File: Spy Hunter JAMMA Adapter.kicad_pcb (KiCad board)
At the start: 2 copper layers, 111.4 x 135.4 mm, 88 parts, among them P1 1K, P2 1K, P3 10K, P4 1K, SW2 SW_DIP_SPSTx02_Slide_9.78x7.2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, U1 74LS86, U10 NE555, U11 LM386, U12 CD4099B, U2 74LS74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

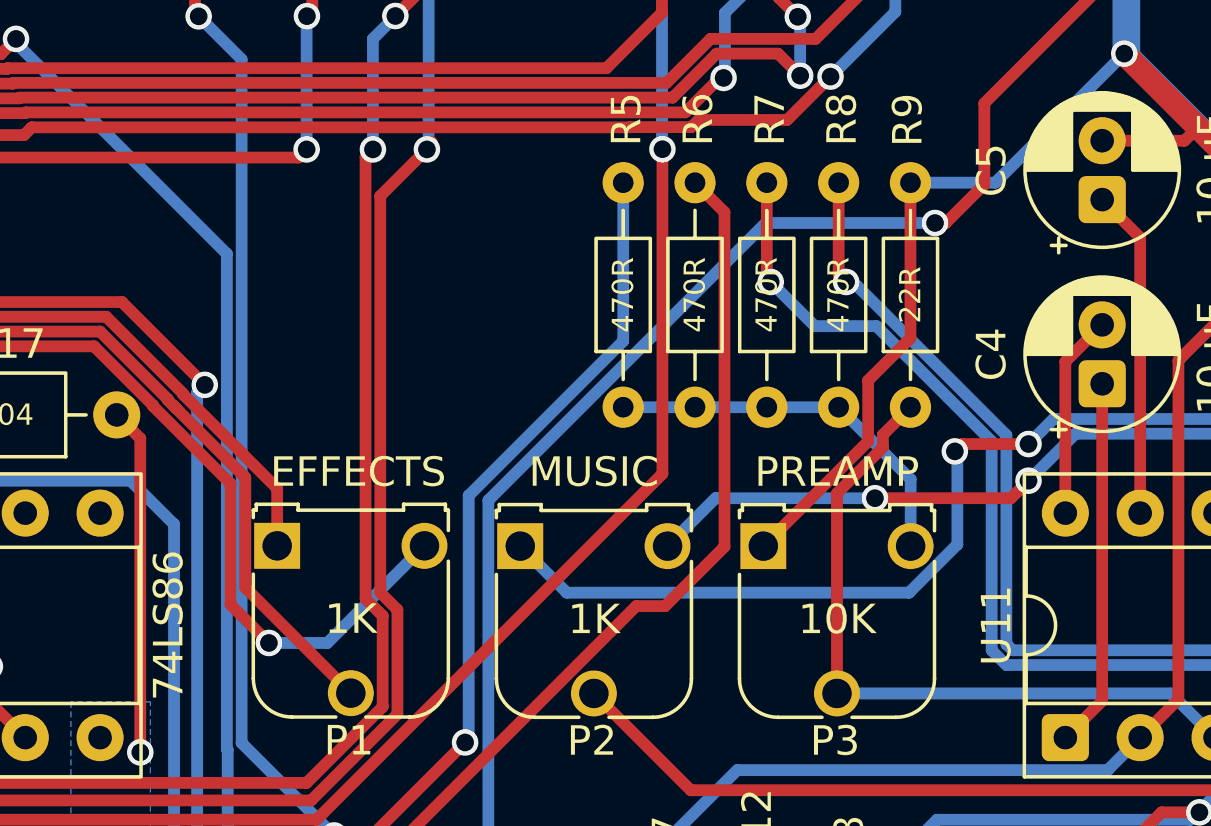
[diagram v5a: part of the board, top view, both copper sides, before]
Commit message: correct polarity of trim pots
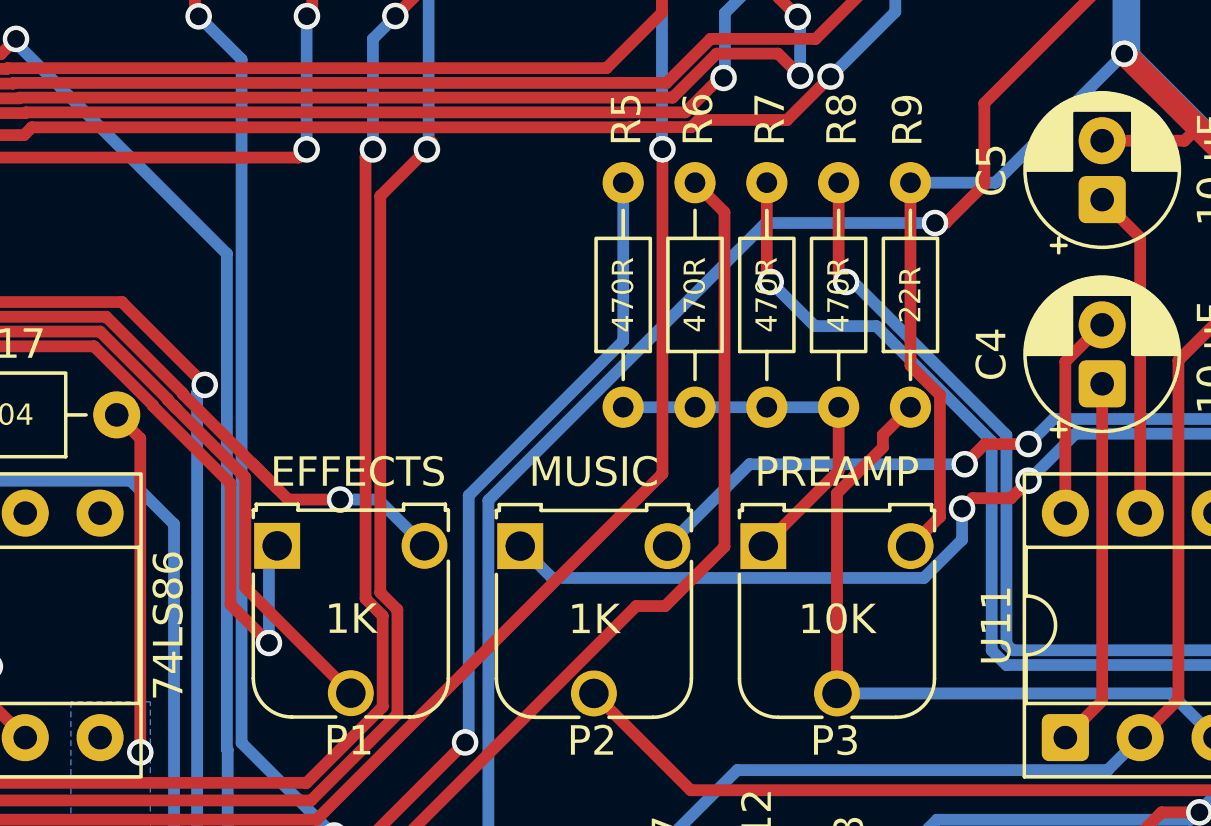
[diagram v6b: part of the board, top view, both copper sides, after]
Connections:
- P1 pad 1: EFFECTS_RVR -> EFFECTS_RV12
- P1 pad 3: EFFECTS_RV12 -> EFFECTS_RVR
- P2 pad 1: MUSIC_RVR -> MUSIC_RV12
- P2 pad 3: MUSIC_RV12 -> MUSIC_RVR
- P3 pad 1: GND -> AUDIO_MONO
- P3 pad 3: AUDIO_MONO -> GND
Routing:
- net MUSIC_RVR: track 115.2 -> 106.9 mm
- net MUSIC_RV12: track 108.7 -> 115.2 mm
- net EFFECTS_RVR: track 52.8 -> 57.8 mm, vias 0 -> 1
- net EFFECTS_RV12: track 63.8 -> 60.5 mm
- net GND: track 1353.4 -> 1352.2 mm
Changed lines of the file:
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@@
 			(layers "*.Cu" "*.Mask")
 			(remove_unused_layers no)
-			(net 7 "EFFECTS_RVR")
+			(net 9 "EFFECTS_RV12")
 		)
 		(pad "2" thru_hole circle
@@
 			(layers "*.Cu" "*.Mask")
 			(remove_unused_layers no)
-			(net 9 "EFFECTS_RV12")
+			(net 7 "EFFECTS_RVR")
 		)
 		(embedded_fonts no)
@@
 			(layers "*.Cu" "*.Mask")
 			(remove_unused_layers no)
-			(net 1 "GND")
+			(net 18 "AUDIO_MONO")
 		)
 		(pad "2" thru_hole circle
@@
 			(layers "*.Cu" "*.Mask")
 			(remove_unused_layers no)
-			(net 18 "AUDIO_MONO")
+			(net 1 "GND")
 		)
 		(embedded_fonts no)
@@
 			(layers "*.Cu" "*.Mask")
 			(remove_unused_layers no)
-			(net 79 "MUSIC_RVR")
+			(net 81 "MUSIC_RV12")
 		)
 		(pad "2" thru_hole circle
@@
 			(layers "*.Cu" "*.Mask")
 			(remove_unused_layers no)
-			(net 81 "MUSIC_RV12")
+			(net 79 "MUSIC_RVR")
 		)
 		(embedded_fonts no)
@@
 	)
 	(segment
-		(start 115.565 56.18)
-		(end 119.122251 52.622749)
-		(width 0.4)
-		(layer "F.Cu")
-		(net 1)
-	)
-	(segment
 		(start 62.155 77.25)
 		(end 63.957106 77.25)
@@
 	)
 	(segment
-		(start 119.122251 52.622749)
-		(end 119.122251 50.557625)
+		(start 121.559751 55.185249)
+		(end 120.565 56.18)
 		(width 0.4)
 		(layer "F.Cu")
@@
 	)
 	(segment
+		(start 120.558751 43.845)
+		(end 120.558751 50.049372)
+		(width 0.4)
+		(layer "F.Cu")
+		(net 1)
+	)
+	(segment
 		(start 133.315 43.965)
 		(end 132.815 44.465)
@@
 	)
 	(segment
+		(start 120.558751 50.049372)
+		(end 121.559751 51.050372)
+		(width 0.4)
+		(layer "F.Cu")
+		(net 1)
+	)
+	(segment
 		(start 163.667498 74.352624)
 		(end 164.2 74.885126)
@@
 	)
 	(segment
-		(start 120.558751 49.121125)
-		(end 120.558751 43.845)
-		(width 0.4)
-		(layer "F.Cu")
-		(net 1)
-	)
-	(segment
 		(start 129.652915 61.382085)
 		(end 129.652915 49.877085)
@@
 	)
 	(segment
+		(start 121.559751 51.050372)
+		(end 121.559751 55.185249)
+		(width 0.4)
+		(layer "F.Cu")
+		(net 1)
+	)
+	(segment
 		(start 129.859888 42.420112)
 		(end 130.315 41.965)
@@
 	)
 	(segment
-		(start 119.122251 50.557625)
-		(end 120.558751 49.121125)
-		(width 0.4)
-		(layer "F.Cu")
-		(net 1)
-	)
-	(segment
 		(start 101.878455 89.359822)
 		(end 99.188277 92.05)
@@
 	)
 	(segment
+		(start 98.220181 53.379819)
+		(end 99.440362 54.6)
+		(width 0.4)
+		(layer "F.Cu")
+		(net 7)
+	)
+	(segment
 		(start 73.461 57.642022)
 		(end 71.186163 59.916859)
@@
 	)
 	(segment
+		(start 99.065 54.224639)
+		(end 98.220181 53.379819)
+		(width 0.4)
+		(layer "F.Cu")
+		(net 7)
+	)
+	(segment
 		(start 76.893889 51.214539)
 		(end 76.88823 51.214539)
@@
 	)
 	(segment
-		(start 99.065 56.17)
-		(end 99.065 54.224639)
+		(start 99.440362 54.6)
+		(end 101.2 54.6)
 		(width 0.4)
 		(layer "F.Cu")
@@
 	)
 	(segment
-		(start 99.065 54.224639)
+		(start 98.220181 53.379819)
 		(end 95.858123 51.017762)
 		(width 0.4)
@@
 		(net 7)
 	)
+	(via
+		(at 101.2 54.6)
+		(size 0.9)
+		(drill 0.6)
+		(layers "F.Cu" "B.Cu")
+		(net 7)
+	)
+	(segment
+		(start 101.2 54.6)
+		(end 102.495 54.6)
+		(width 0.4)
+		(layer "B.Cu")
+		(net 7)
+	)
+	(segment
+		(start 102.495 54.6)
+		(end 104.065 56.17)
+		(width 0.4)
+		(layer "B.Cu")
+		(net 7)
+	)
 	(segment
 		(start 73.963 57.849958)
@@
 	)
 	(segment
-		(start 100.768679 59.466321)
-		(end 98.785149 59.466321)
+		(start 98.785149 56.449851)
+		(end 99.065 56.17)
 		(width 0.4)
 		(layer "B.Cu")
@@
 	)
 	(segment
-		(start 104.065 56.17)
-		(end 100.768679 59.466321)
+		(start 98.785149 59.466321)
+		(end 98.785149 56.449851)
 		(width 0.4)
 		(layer "B.Cu")
@@
 	)
 	(segment
-		(start 120.565 53.908749)
-		(end 120.565 56.18)
+		(start 118.121251 51.465)
+		(end 118.121251 53.623749)
 		(width 0.4)
-		(layer "B.Cu")
+		(layer "F.Cu")
 		(net 18)
 	)
 	(segment
-		(start 118.121251 51.465)
-		(end 120.565 53.908749)
+		(start 118.121251 53.623749)
+		(end 115.565 56.18)
 		(width 0.4)
-		(layer "B.Cu")
+		(layer "F.Cu")
 		(net 18)
 	)
@@
 	)
 	(segment
+		(start 123.085 52.715)
+		(end 122.4 53.4)
+		(width 0.4)
+		(layer "F.Cu")
+		(net 79)
+	)
+	(segment
 		(start 151.765 101.265)
 		(end 149.4 98.9)
@@
 	(segment
 		(start 124.565 52.715)
-		(end 122.315 52.715)
-		(width 0.4)
-		(layer "F.Cu")
-		(net 79)
-	)
-	(segment
-		(start 122.315 52.715)
-		(end 122.065 52.965)
+		(end 123.085 52.715)
 		(width 0.4)
 		(layer "F.Cu")
@@
 	)
 	(via
-		(at 122.065 52.965)
+		(at 122.4 53.4)
 		(size 0.9)
 		(drill 0.6)
@@
 	)
 	(segment
-		(start 122.15 56.123765)
-		(end 120.512765 57.761)
-		(width 0.4)
-		(layer "B.Cu")
-		(net 79)
-	)
-	(segment
-		(start 122.15 53.05)
-		(end 122.15 56.123765)
+		(start 115.095 53.4)
+		(end 112.315 56.18)
 		(width 0.4)
 		(layer "B.Cu")
@@
 	)
 	(segment
-		(start 120.512765 57.761)
-		(end 108.896 57.761)
-		(width 0.4)
-		(layer "B.Cu")
-		(net 79)
-	)
-	(segment
 		(start 153.365 103.865)
 		(end 151.765 102.265)
@@
 	)
 	(segment
-		(start 108.896 57.761)
-		(end 107.315 56.18)
+		(start 122.4 53.4)
+		(end 115.095 53.4)
 		(width 0.4)
 		(layer "B.Cu")
@@
 	)
 	(segment
-		(start 122.065 52.965)
-		(end 122.15 53.05)
-		(width 0.4)
-		(layer "B.Cu")
-		(net 79)
-	)
-	(segment
 		(start 113.1 64.465)
 		(end 142.815 64.465)
@@
 	)
 	(segment
-		(start 123.9705 54.5535)
-		(end 119.3535 54.5535)
-		(width 0.4)
-		(layer "F.Cu")
-		(net 81)
-	)
-	(segment
 		(start 148.9 99.3)
 		(end 148.9 90.77868)
@@
 	)
 	(segment
-		(start 124.565 53.959)
-		(end 123.9705 54.5535)
+		(start 122.663332 54.5535)
+		(end 122.309751 54.907081)
 		(width 0.4)
 		(layer "F.Cu")
@@
 	)
 	(segment
+		(start 123.9705 54.5535)
+		(end 122.663332 54.5535)
+		(width 0.4)
+		(layer "F.Cu")
+		(net 81)
+	)
+	(segment
 		(start 148.165 88.490171)
 		(end 148.176645 88.478526)
@@
 		(net 81)
 	)
+	(segment
+		(start 124.565 53.959)
+		(end 123.9705 54.5535)
+		(width 0.4)
+		(layer "F.Cu")
+		(net 81)
+	)
 	(via
 		(at 150.631667 101.586997)
@@
 	)
 	(via
-		(at 119.3535 54.5535)
+		(at 122.309751 54.907081)
 		(size 0.9)
 		(drill 0.6)
@@
 	)
 	(segment
-		(start 112.315 56.18)
-		(end 113.9415 54.5535)
+		(start 121.012765 57.261)
+		(end 108.396 57.261)
 		(width 0.4)
 		(layer "B.Cu")
@@
 	)
 	(segment
+		(start 122.309751 54.907081)
+		(end 122.309751 55.964014)
+		(width 0.4)
+		(layer "B.Cu")
+		(net 81)
+	)
+	(segment
 		(start 150.631667 101.653664)
 		(end 150.565 101.586997)
@@
 	)
 	(segment
-		(start 113.9415 54.5535)
-		(end 119.3535 54.5535)
+		(start 148.165 86.930817)
+		(end 148.165 86.930823)
 		(width 0.4)
 		(layer "B.Cu")
@@
 	)
 	(segment
-		(start 148.165 86.930817)
-		(end 148.165 86.930823)
+		(start 159.4 127.48)
+		(end 153.665 121.745)
 		(width 0.4)
 		(layer "B.Cu")
@@
 	)
 	(segment
-		(start 159.4 127.48)
-		(end 153.665 121.745)
+		(start 108.396 57.261)
+		(end 107.315 56.18)
 		(width 0.4)
 		(layer "B.Cu")
@@
 		(width 0.4)
 		(layer "B.Cu")
+		(net 81)
+	)
+	(segment
+		(start 122.309751 55.964014)
+		(end 121.012765 57.261)
+		(width 0.4)
+		(layer "B.Cu")

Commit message: minor cleanup and fine tuning
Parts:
- moved CR2450 0.80 mm to (105.2, 147.4)
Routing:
- net J5_ST0: track 102.9 -> 101.0 mm
- net EFFECTS_RVR: track 57.8 -> 56.6 mm
- net BATT+: track 85.3 -> 84.5 mm
- net GND: track 1352.2 -> 1351.4 mm
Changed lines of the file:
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@@
 		(tags "Resistor Axial_DIN0204 series Axial Horizontal pin pitch 7.62mm 0.167W length 3.6mm diameter 1.6mm")
 		(property "Reference" "R16"
-			(at 10.335 0 0)
+			(at 3.735 -2 0)
 			(layer "F.SilkS")
 			(effects
@@
 	(footprint "Battery:BatteryHolder_ComfortableElectronic_CH273-2450_1x2450"
 		(layer "F.Cu")
-		(at 104.4 147.4)
+		(at 105.2 147.4)
 		(descr "Comfortable Electronic CR2450 battery holder, http://www.comf.com.tw/ProductDetail.asp?no=148")
 		(tags "Comfortable Electronic CR2450")
@@
 	)
 	(segment
+		(start 132.215 147.4)
+		(end 134.2 145.415)
+		(width 0.4)
+		(layer "F.Cu")
+		(net 1)
+	)
+	(segment
 		(start 146.962582 148.297895)
 		(end 146.774846 148.297895)
@@
 	)
 	(segment
-		(start 132.215 147.4)
-		(end 134.2 145.415)
-		(width 0.4)
-		(layer "F.Cu")
-		(net 1)
-	)
-	(segment
 		(start 89.891275 39.983445)
 		(end 63.133445 39.983445)
@@
 	)
 	(segment
-		(start 101.878455 89.359822)
-		(end 99.188277 92.05)
+		(start 125.2 147.4)
+		(end 132.215 147.4)
 		(width 0.4)
 		(layer "F.Cu")
@@
 	)
 	(segment
-		(start 124.4 147.4)
-		(end 132.215 147.4)
+		(start 101.878455 89.359822)
+		(end 99.188277 92.05)
 		(width 0.4)
 		(layer "F.Cu")
@@
 	)
 	(segment
-		(start 99.065 54.224639)
-		(end 98.220181 53.379819)
-		(width 0.4)
-		(layer "F.Cu")
-		(net 7)
-	)
-	(segment
 		(start 76.893889 51.214539)
 		(end 76.88823 51.214539)
@@
 	)
 	(segment
-		(start 131.765 144.665)
-		(end 132.565 145.465)
+		(start 149.384414 138.7)
+		(end 149.592207 138.7)
 		(width 0.4)
 		(layer "F.Cu")
@@
 	)
 	(segment
-		(start 149.384414 138.7)
-		(end 149.592207 138.7)
+		(start 111.23 147.4)
+		(end 113.965 144.665)
 		(width 0.4)
 		(layer "F.Cu")
@@
 	)
 	(segment
-		(start 139.304568 145.193907)
-		(end 139.675661 145.565)
+		(start 131.765 144.665)
+		(end 132.565 145.465)
 		(width 0.4)
 		(layer "F.Cu")
@@
 	)
 	(segment
-		(start 104.4 147.4)
-		(end 111.23 147.4)
+		(start 139.304568 145.193907)
+		(end 139.675661 145.565)
 		(width 0.4)
 		(layer "F.Cu")
@@
 	)
 	(segment
-		(start 111.23 147.4)
-		(end 113.965 144.665)
+		(start 142.519414 145.565)
+		(end 149.384414 138.7)
 		(width 0.4)
 		(layer "F.Cu")
@@
 	)
 	(segment
-		(start 142.519414 145.565)
-		(end 149.384414 138.7)
+		(start 139.675661 145.565)
+		(end 142.519414 145.565)
 		(width 0.4)
 		(layer "F.Cu")
@@
 	)
 	(segment
-		(start 139.675661 145.565)
-		(end 142.519414 145.565)
+		(start 105.2 147.4)
+		(end 111.23 147.4)
 		(width 0.4)
 		(layer "F.Cu")
@@
 	)
 	(segment
-		(start 62.155 142.585)
-		(end 63.987893 142.585)
+		(start 63.987893 142.585)
+		(end 73.802894 152.4)
 		(width 0.4)
 		(layer "B.Cu")
@@
 	)
 	(segment
-		(start 74.84514 99.3)
-		(end 79.44402 99.3)
+		(start 149.83 152.4)
+		(end 157.23 145)
 		(width 0.4)
 		(layer "B.Cu")
@@
 	)
 	(segment
-		(start 63.987893 142.585)
-		(end 73.802894 152.4)
+		(start 74.84514 99.3)
+		(end 79.44402 99.3)
 		(width 0.4)
 		(layer "B.Cu")
@@
 	)
 	(segment
-		(start 159.12 144.6)
-		(end 159.4 144.88)
+		(start 157.23 145)
+		(end 159.28 145)
 		(width 0.4)
 		(layer "B.Cu")
@@
 	)
 	(segment
-		(start 149.83 152.4)
-		(end 157.63 144.6)
+		(start 74.23014 99.915)
+		(end 74.84514 99.3)
 		(width 0.4)
 		(layer "B.Cu")
@@
 	)
 	(segment
-		(start 157.63 144.6)
-		(end 159.12 144.6)
+		(start 73.802894 152.4)
+		(end 149.83 152.4)
 		(width 0.4)
 		(layer "B.Cu")
@@
 	)
 	(segment
-		(start 74.23014 99.915)
-		(end 74.84514 99.3)
+		(start 62.155 142.585)
+		(end 63.987893 142.585)
 		(width 0.4)
 		(layer "B.Cu")
@@
 	)
 	(segment
-		(start 73.802894 152.4)
-		(end 149.83 152.4)
+		(start 159.28 145)
+		(end 159.4 144.88)
 		(width 0.4)
 		(layer "B.Cu")
@@
 	)
 	(segment
-		(start 73.595787 152.9)
-		(end 65.820787 145.125)
+		(start 81.391568 100.258807)
+		(end 81.391568 99.589322)
 		(width 0.4)
 		(layer "B.Cu")
@@
 	)
 	(segment
-		(start 81.391568 100.258807)
-		(end 81.391568 99.589322)
+		(start 159.4 147.42)
+		(end 155.591223 147.42)
 		(width 0.4)
 		(layer "B.Cu")
@@
 	)
 	(segment
-		(start 158.98 147)
-		(end 156.011223 147)
+		(start 73.595787 152.9)
+		(end 65.820787 145.125)
 		(width 0.4)
 		(layer "B.Cu")
@@
 	)
 	(segment
-		(start 159.4 147.42)
-		(end 158.98 147)
+		(start 155.591223 147.42)
+		(end 150.111223 152.9)
 		(width 0.4)
 		(layer "B.Cu")
@@
 	)
 	(segment
-		(start 156.011223 147)
-		(end 150.111223 152.9)
-		(width 0.4)
-		(layer "B.Cu")
-		(net 96)
-	)
-	(segment
 		(start 58.2 110.935987)
 		(end 58.599 110.536987)
@@
 	)
 	(segment
-		(start 159.4 148.76)
-		(end 159.265 148.625)
-		(width 0.4)
-		(layer "B.Cu")
-		(net 100)
-	)
-	(segment
 		(start 73.358418 153.4)
 		(end 67.623418 147.665)
@@
 	)
 	(segment
-		(start 155.175 148.625)
+		(start 153.84 149.96)
 		(end 150.4 153.4)
 		(width 0.4)
@@
 	)
 	(segment
-		(start 159.4 149.96)
-		(end 159.4 148.76)
-		(width 0.4)
-		(layer "B.Cu")
-		(net 100)
-	)
-	(segment
 		(start 67.623418 147.665)
 		(end 62.155 147.665)
@@
 	)
 	(segment
-		(start 159.265 148.625)
-		(end 155.175 148.625)
+		(start 159.4 149.96)
+		(end 153.84 149.96)
 		(width 0.4)
 		(layer "B.Cu")
